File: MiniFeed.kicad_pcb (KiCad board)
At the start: 2 copper layers, 100 x 44.4 mm, 77 parts, among them J1 Connector_1, J2 Uart, J3 Debug, J4 Connector_2, M1 Motor_DC, SW1 SW_-, SW2 SW_S, SW3 SW_+, SW4 Detect1, SW5 Detect2, U1 TLV1117-33, U2 DRV8876, U3 STM32G031KxT, U4 VCNT2020, U5 VG-7240TSWEG02, U6 VCNT2020

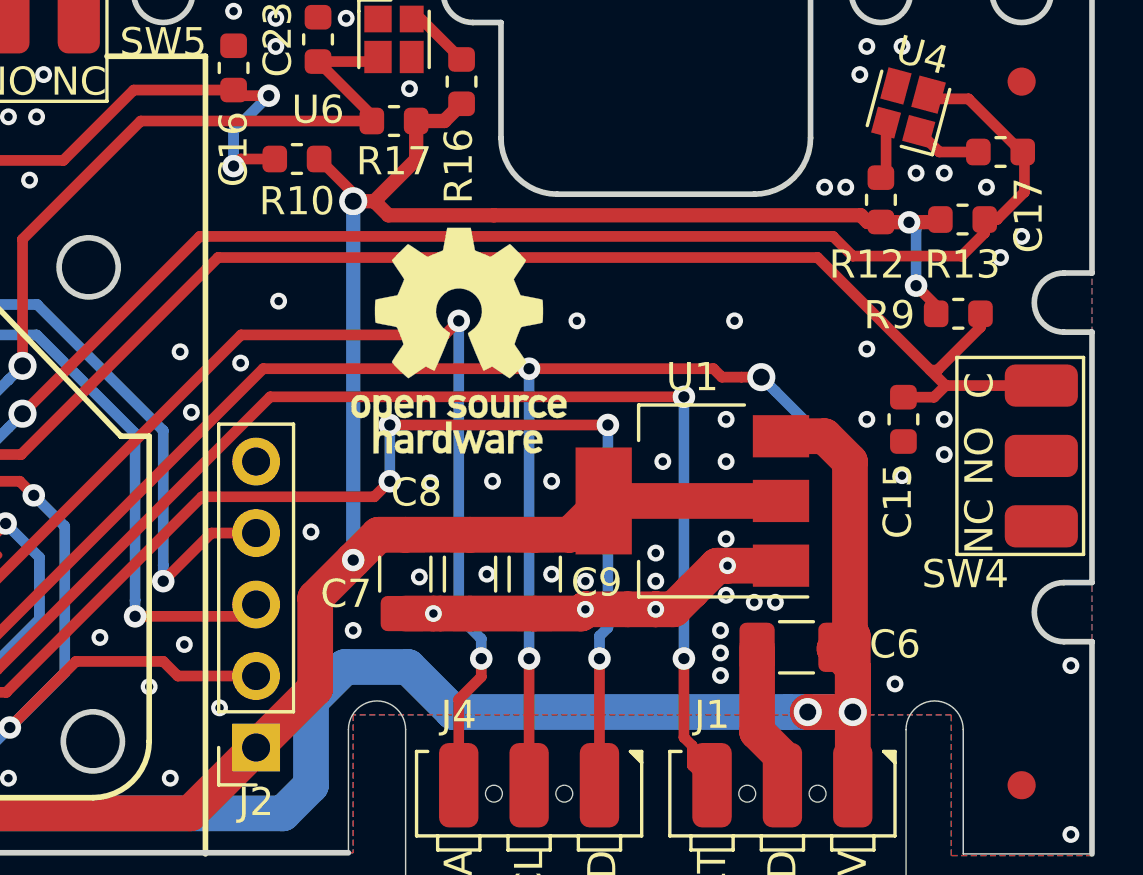
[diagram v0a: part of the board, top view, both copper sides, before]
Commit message: Fixed LDO design: Added resistor to increase ESR for LDO. Added diode to LDO to protect the regulator if the input instantaneously is shorted to GND.
Fixed the SCL trace.
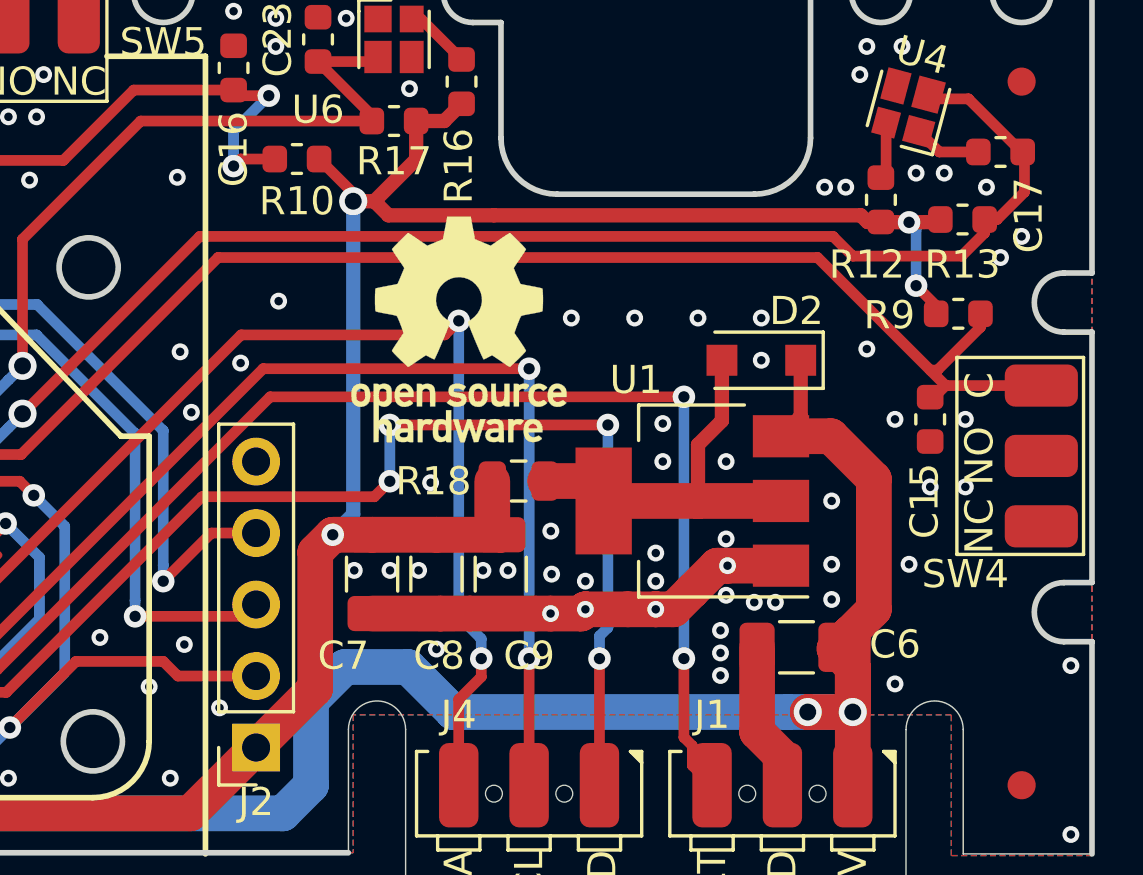
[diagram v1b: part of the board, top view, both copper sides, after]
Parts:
- added D2: 1N4002, Diode_SMD:D_SOD-123F, F.Cu at (173.8, 91.4)
- added R18: 0R5, Resistor_SMD:R_0805_2012Metric, F.Cu at (165.1, 95.7)
- moved C9 1.21 mm to (164.5, 99.0)
- moved C8 1.19 mm to (162.2, 99.0)
- moved C7 1.18 mm to (159.9, 99.0)
- moved C15 0.95 mm to (179.8, 93.5)
- moved REF** 0.40 mm to (163.0, 90.3)
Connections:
- U1 pad 2: +3V3 -> Net-(D2-Pad2)
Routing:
- net Net-(D2-Pad2): track 0.00 -> 14.0 mm
- net /SCL: track 51.9 -> 41.4 mm, vias 3 -> 2
- net +3V3: track 253.6 -> 244.8 mm
- net +12V: track 107.5 -> 111.4 mm
- net GND: track 50.7 -> 51.9 mm, vias 170 -> 179
- net /TapeDetect: track 47.3 -> 46.3 mm
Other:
- board text added: "v0.2"
- board text removed: "v0.1"

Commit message: Updated PCB design
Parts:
- removed  : Fiducial_1mm_Mask2mm, Fiducial:Fiducial_1mm_Mask2mm
- removed the C15 at (179.8, 93.5)
- removed the C24 at (98.8, 87.2)
- removed the C8 at (162.2, 99.0)
- removed the C9 at (164.5, 99.0)
- removed D2: 1N4002, Diode_SMD:D_SOD-123F
- removed the R18 at (165.1, 95.7)
- removed the U1 at (171.3, 96.4)
- added C14: 100n, Capacitor_SMD:C_0603_1608Metric, F.Cu at (155.0, 81.0)
- added C21: 1u, Capacitor_SMD:C_0603_1608Metric, F.Cu at (97.9, 89.0)
- added C28: DNP, Capacitor_SMD:C_0603_1608Metric, F.Cu at (169.9, 90.7)
- added C29: DNP, Capacitor_SMD:C_0603_1608Metric, F.Cu at (176.4, 88.1)
- added C4: 100n, Capacitor_SMD:C_0603_1608Metric, F.Cu at (160.1, 95.2)
- added C5: 100n, Capacitor_SMD:C_0603_1608Metric, F.Cu at (109.7, 105.4)
- added R2: 10k, Resistor_SMD:R_0603_1608Metric, F.Cu at (168.0, 101.3)
- added R24: 150R, Resistor_SMD:R_0603_1608Metric, F.Cu at (163.1, 87.4)
- added R25: 10k, Resistor_SMD:R_0603_1608Metric, F.Cu at (169.9, 89.0)
- added R26: 150R, Resistor_SMD:R_0603_1608Metric, F.Cu at (169.9, 87.4)
- added R27: 10k, Resistor_SMD:R_0603_1608Metric, F.Cu at (178.1, 88.8)
- added R4: 4k7, Resistor_SMD:R_0603_1608Metric, F.Cu at (132.9, 94.9)
- added R6: 4k7, Resistor_SMD:R_0603_1608Metric, F.Cu at (133.0, 96.8)
- added R7: 4k7, Resistor_SMD:R_0603_1608Metric, F.Cu at (133.0, 98.6)
- added R8: 4k7, Resistor_SMD:R_0603_1608Metric, F.Cu at (134.5, 102.0)
- added R9: 4k7, Resistor_SMD:R_0603_1608Metric, F.Cu at (133.0, 100.2)
- added U2: M24C32, Package_SO:SOIC-8_3.9x4.9mm_P1.27mm, F.Cu at (114.4, 103.9)
- added U4: USBLC6-2SC6, Package_TO_SOT_SMD:SOT-23-6, F.Cu at (164.6, 101.3)
- added U8: VCNT2020, global:vcnt2020, F.Cu at (166.4, 88.6)
- added U9: VCNT2020, global:vcnt2020, F.Cu at (173.6, 88.6)
- C1: value 10u -> 2u2; footprint Capacitor_SMD:C_1206_3216Metric -> Capacitor_SMD:C_0805_2012Metric
- C22: value 1u -> 2u2; footprint Capacitor_SMD:C_0603_1608Metric -> Capacitor_SMD:C_0805_2012Metric
- Fid1, Fid2, Fid3, Fid4, Fid5: renamed from  
- G1: renamed from G***; value LOGO -> CC
- G2: renamed from G***; value LOGO -> BY
- G3: renamed from REF**; value OSHW-Logo_7.5x8mm_SilkScreen -> OSHW-Logo_5.7x6mm_SilkScreen; footprint Symbol:OSHW-Logo_7.5x8mm_SilkScreen -> Symbol:OSHW-Logo_5.7x6mm_SilkScreen
- G4: renamed from G***; value LOGO -> SG-O
- R10: renamed from R3; value 4k7 -> 1k
- SW1, SW2, SW3: footprint global:TS36CA-0.7 -> global:SW_SPST_TS-1065A-B3D4
- U5: footprint global:VG-7240TSWEG02 -> global:VG-7240TSWEG02-mirror
- moved SW5 39.1 mm to (183.1, 94.8), turned to 270 degrees
- moved SW4 39.1 mm to (147.0, 80.0), turned to 0 degrees
- moved R19 33.1 mm to (130.4, 75.4), turned to 90 degrees
- moved C15 27.8 mm to (179.7, 93.7), turned to 270 degrees
- moved R15 24.2 mm to (157.2, 84.3), turned to 180 degrees
- moved R16 22.6 mm to (177.4, 94.4), turned to 0 degrees
- moved C25 18.5 mm to (98.1, 103.7), turned to 0 degrees
- moved C24 16.8 mm to (98.1, 101.8)
- moved C23 13.3 mm to (97.9, 100.0)
- moved C20 13.2 mm to (94.6, 86.9), turned to 180 degrees
- moved C16 12.3 mm to (172.2, 98.3), turned to 0 degrees
- moved SW3 10.6 mm to (116.0, 76.9)
- moved R12 10.2 mm to (121.0, 77.9), turned to 180 degrees
- moved C17 8.96 mm to (99.7, 89.3), turned to 90 degrees
- moved SW2 7.62 mm to (108.6, 78.2)
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- renumbered C12 to C11, C13 to C12, C14 to C13, C16 to C15, C7 to C16, C18 to C17, C19 to C18, C20 to C19, C21 to C20, C25 to C23, C26 to C24, C27 to C25, C17 to C26, C23 to C27, C11 to C3, C3 to C6, C4 to C7, C5 to C8, C6 to C9, J3 to J1, J1 to J2, J2 to J3, Mech to Mech1, Mech to Mech2, Mech to Mech3, R4 to R11, R6 to R12, R7 to R13, R8 to R14, R9 to R15, R10 to R16, R14 to R17, R15 to R18, R11 to R19, R12 to R20, R13 to R21, R16 to R22, R17 to R23, R5 to R3, R2 to R5, U3 to U1, U2 to U3, U4 to U6, U6 to U7
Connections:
- C22 pad 2: Net-(C22-Pad2) -> GND
- J2 pad 3: /FaultOut -> +3V3
- J4 pad 2: /SCL -> Net-(J4-Pad2)
- J4 pad 3: /SDA -> Net-(J4-Pad3)
- R10 pad 1: /M_ISense -> Net-(R10-Pad1)
- R5 pad 2: /M_Fault -> Net-(R5-Pad2)
- U1 pad 12: (no net) -> /SensorB
- U1 pad 14: /SensorB -> /SensorC
- U1 pad 17: /ID -> Net-(C4-Pad1)
- U1 pad 18: /FaultOut -> /SensorD
- U1 pad 19: /SCL -> /TX
- U1 pad 2: (no net) -> GND
- U1 pad 21: /SDA -> /RX
- U1 pad 26: /TapeDetect -> /OptDetect
- U1 pad 27: /OptDetect -> /TapeDetect
- U1 pad 30: /TX -> /SCL
- U1 pad 31: /RX -> /SDA
- U3 pad 1: /M_EN -> Net-(R4-Pad1)
- U3 pad 2: /M_PH -> Net-(R6-Pad1)
- U3 pad 3: /M_Sleep -> Net-(R7-Pad1)
- U3 pad 4: /M_Fault -> Net-(R5-Pad2)
- U3 pad 6: /M_ISense -> Net-(R10-Pad1)
- U5 pad 15: Net-(C24-Pad1) -> Net-(C22-Pad1)
- U5 pad 3: Net-(C22-Pad1) -> Net-(C21-Pad1)
- U5 pad 4: Net-(C22-Pad2) -> Net-(C21-Pad2)
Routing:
- net /SensorD: track 0.00 -> 48.3 mm, vias 0 -> 2
- net /FaultOut: track 46.9 -> 0.00 mm, vias 2 -> 0
- net /SensorC: track 0.00 -> 41.1 mm, vias 0 -> 2
- net /ID: track 44.7 -> 4.40 mm, vias 4 -> 0
- net Net-(C4-Pad1): track 0.00 -> 36.1 mm, vias 0 -> 4
- net Net-(D1-Pad2): track 3.08 -> 36.8 mm
- net /LED: track 56.9 -> 26.9 mm, vias 6 -> 0
- net /OLED_SCL: track 67.0 -> 95.2 mm, vias 2 -> 6
- net /OLED_SDA: track 74.5 -> 95.2 mm, vias 2 -> 6
- net /M_EN: track 23.5 -> 3.35 mm, vias 2 -> 0
- net /M_PH: track 22.9 -> 2.82 mm, vias 2 -> 0
- net /M_Sleep: track 22.0 -> 2.75 mm, vias 2 -> 0
- net /M_Fault: track 22.9 -> 3.75 mm
- net Net-(R5-Pad2): track 0.00 -> 18.8 mm
- net Net-(R6-Pad1): track 0.00 -> 18.6 mm, vias 0 -> 2
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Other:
- board text added: "3.3V"
- board text added: "v1.0"
- board text removed: "FAULT"
- board text removed: "v0.2"
